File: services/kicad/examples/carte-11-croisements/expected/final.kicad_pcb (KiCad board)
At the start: 2 copper layers, 90 x 60 mm, 6 parts, among them J1 BUS_A, J2 BUS_B

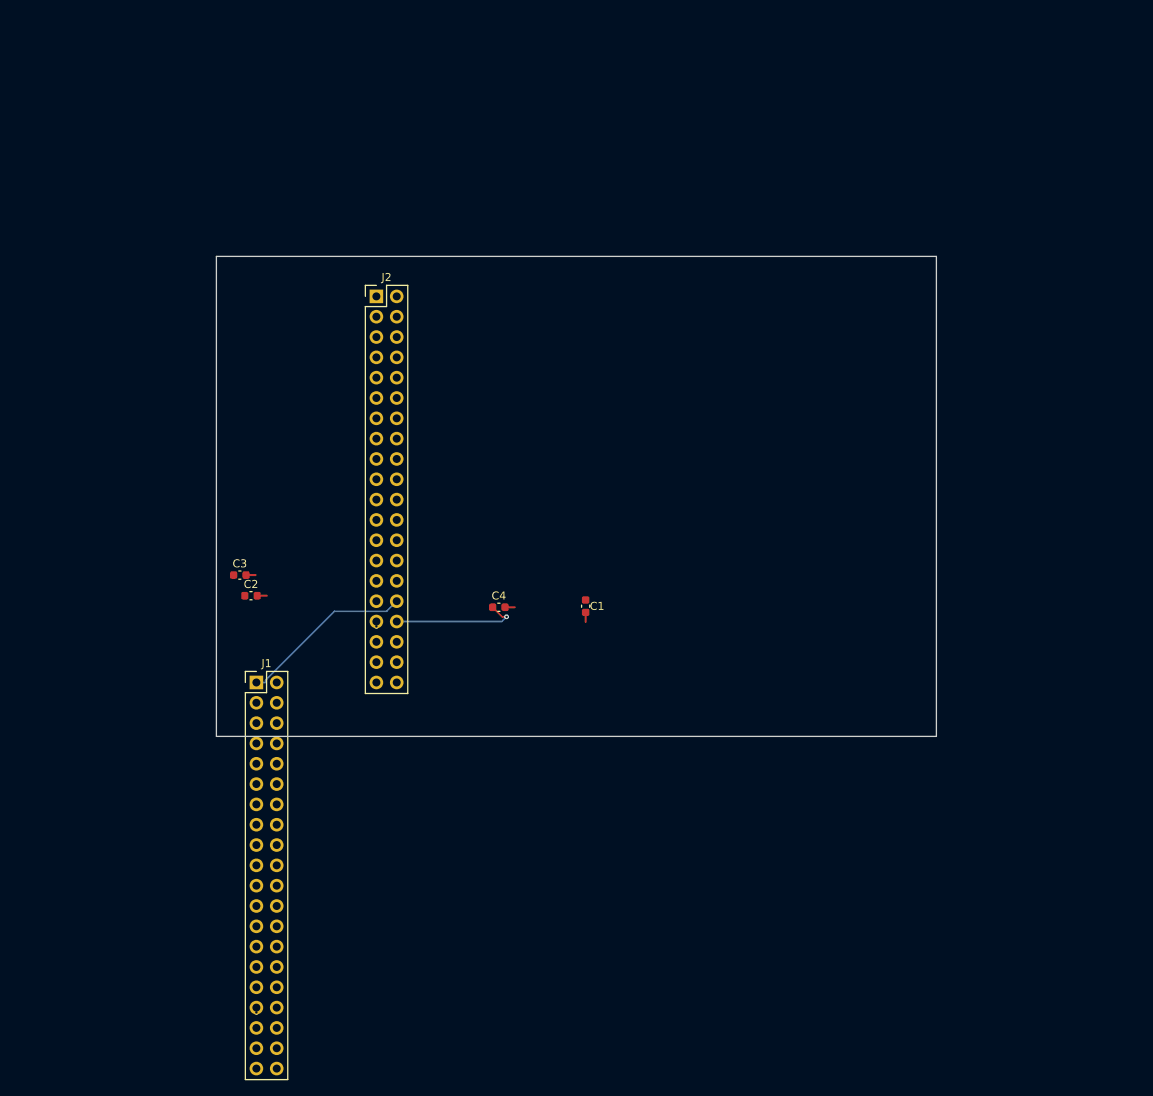
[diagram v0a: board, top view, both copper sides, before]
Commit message: feat(kicad): placement pro et routage 100 % fabricable sur les 16 cartes -- integration sur main (#164)
Branche d'integration coupee depuis origin/main (fab2a82, PR #162) : les
fichiers cles de main etaient des instantanes de feat/placement-seed-snap-
bypass (routing.py = 7981019, placement.py = 437a8b4...). On reprend donc
l'arbre entier de cette branche (345 commits, dernier 9f48667) et on y
conserve ce que main seul apportait :
- tools/verrou_routage.py + son test : « 6,2 Go par routage » rectifie
  (0,2 Go mesure ; c'est la concurrence qui emballe la memoire) ;
- tests/test_driver_llm_resync.py ;
- CLAUDE.md, PLAN.md, DECISIONS.md : fusion a trois voies, les sections
  des deux lignes conservees (2026-09-05 conteneur/verrou, 2026-09-07
  parcours asynchrone et chaine du driver, 2026-09-09/10 lecons).
Les skills *-delegate restent supprimes (remplaces le 2026-08-30).

Contenu : banc en deux phases (placement valide puis routage gele), snap
sur les regles natives, repli GND cible, journal Freerouting incremental,
horloge sans progres, via d'echappement vers le plan principal,
serigraphie degagee ; 16 cartes livrees a 100 %, 0 erreur DRC.

Verification : pytest services/kicad 1805 passed, 16 skipped ;
pnpm type-check 8/8.


Claude-Session: https://claude.ai/code/session_01TnMqm4La2CxQHHB5K8aSSV

Co-authored-by: Claude Fable 5.1 <noreply@anthropic.com>
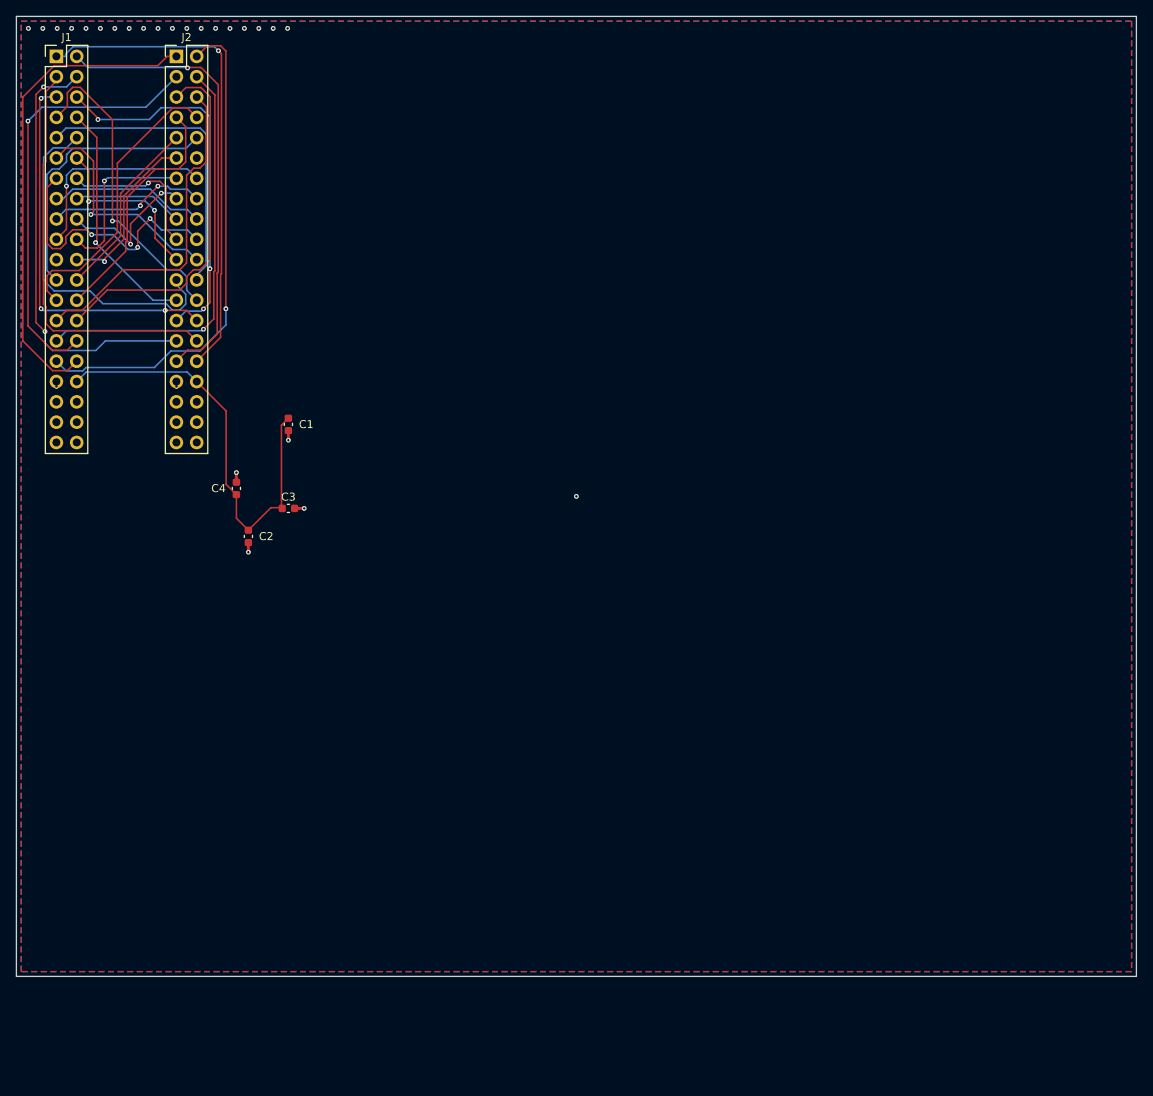
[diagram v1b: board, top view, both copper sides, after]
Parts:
- moved J1 82.2 mm to (83.5, 50.0)
- moved C1 43.6 mm to (112.5, 96.0)
- moved J2 39.1 mm to (98.5, 50.0)
- moved C4 36.0 mm to (106.0, 104.0), turned to 90 degrees
- moved C3 10.3 mm to (112.5, 106.5)
- moved C2 7.42 mm to (107.5, 110.0), turned to -90 degrees
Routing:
- net X31: track 0.00 -> 62.8 mm, vias 0 -> 1
- net X32: track 0.00 -> 60.5 mm
- net X02: track 0.00 -> 56.9 mm, vias 0 -> 1
- net X04: track 0.00 -> 54.9 mm, vias 0 -> 2
- net X30: track 0.00 -> 54.3 mm, vias 0 -> 1
- net X29: track 0.00 -> 52.1 mm, vias 0 -> 1
- net X03: track 0.00 -> 51.4 mm
- net X05: track 0.00 -> 48.5 mm, vias 0 -> 3
- net X06: track 0.00 -> 47.3 mm, vias 0 -> 3
- net X28: track 0.00 -> 45.9 mm
- net X10: track 0.00 -> 43.6 mm
- net X27: track 0.00 -> 42.0 mm
- net X07: track 0.00 -> 39.5 mm, vias 0 -> 1
- net X01: track 21.9 -> 61.4 mm, vias 0 -> 1
- net X09: track 0.00 -> 38.3 mm
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- added copper zone on B.Cu, net GND
- added copper zone on F.Cu, net GND
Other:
- board size 90 x 60 mm -> 140 x 120 mm
- copper layers 2 -> 4

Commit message: banc(rejeu): douze cartes hors le banc des dix, et le trou qu elles ont revele
Demande : refaire placement et routage de toutes les cartes d `examples/`
SAUF les dix du banc, sans toucher `stm32-validation` ni `STM32-Test`.

DOUZE CARTES REJOUEES, DEUX FAMILLES.

  groupe A (input/schema.json)        regenerer_le_banc.py — garde le meilleur
      carte-11-croisements            100 % · 0 err · 0 perdu   GARDE
      driver-clignotant-ne555         100 % · 0 err · 0 perdu   GARDE
      driver-stm32-minimal            100 % · 0 err · 0 perdu   GARDE
      driver-thermometre-i2c          100 % · 0 err · 0 perdu   GARDE

  groupe B (input/circuit.json)       banc_exemples.py — ecrit dans output/
      arduino-uno       2 couches  100 %  0 manq  0 err    925 s
      esp32-baseline    2 couches  100 %  0 manq  0 err    387 s
      led-blinker       2 couches  100 %  0 manq  0 err    124 s
      nucleo-f401       4 couches   98 %  1 manq  0 err   1814 s
      stm32-baseline    2 couches  100 %  0 manq  0 err    193 s
      stm32-30          2 couches  100 %  0 manq  0 err    404 s
      stm32-60          2 couches  100 %  0 manq  0 err    414 s
      stm32-100         2 couches  100 %  0 manq  0 err    308 s

LE REJEU CONFIRME LES BOARDS LIVRES — ON NE REMPLACE RIEN.

DRC des boards VERSIONNES face aux boards du rejeu, meme instrument
(`kicad-cli pcb drc --severity-all`) des deux cotes :

      sept cartes            0 err · 0 manq des DEUX cotes   egalite
      nucleo-f401            0 manq versionne, 1 au rejeu    on garde l ancien

Livrer des boards de qualite identique ferait du bruit sans rien apporter, et
le tirage de `nucleo-f401` est moins bon : la protection a joue exactement
comme prevu.

LE TROU : CES HUIT CARTES N AVAIENT AUCUN `mesures.json`.

Leur board etait livre depuis le 2026-09-07 et RIEN ne disait ce qu il valait.
Un lecteur ne pouvait ni le verifier ni s en apercevoir — c est la faute que ce
depot poursuit partout, appliquee non pas a un compteur mais a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
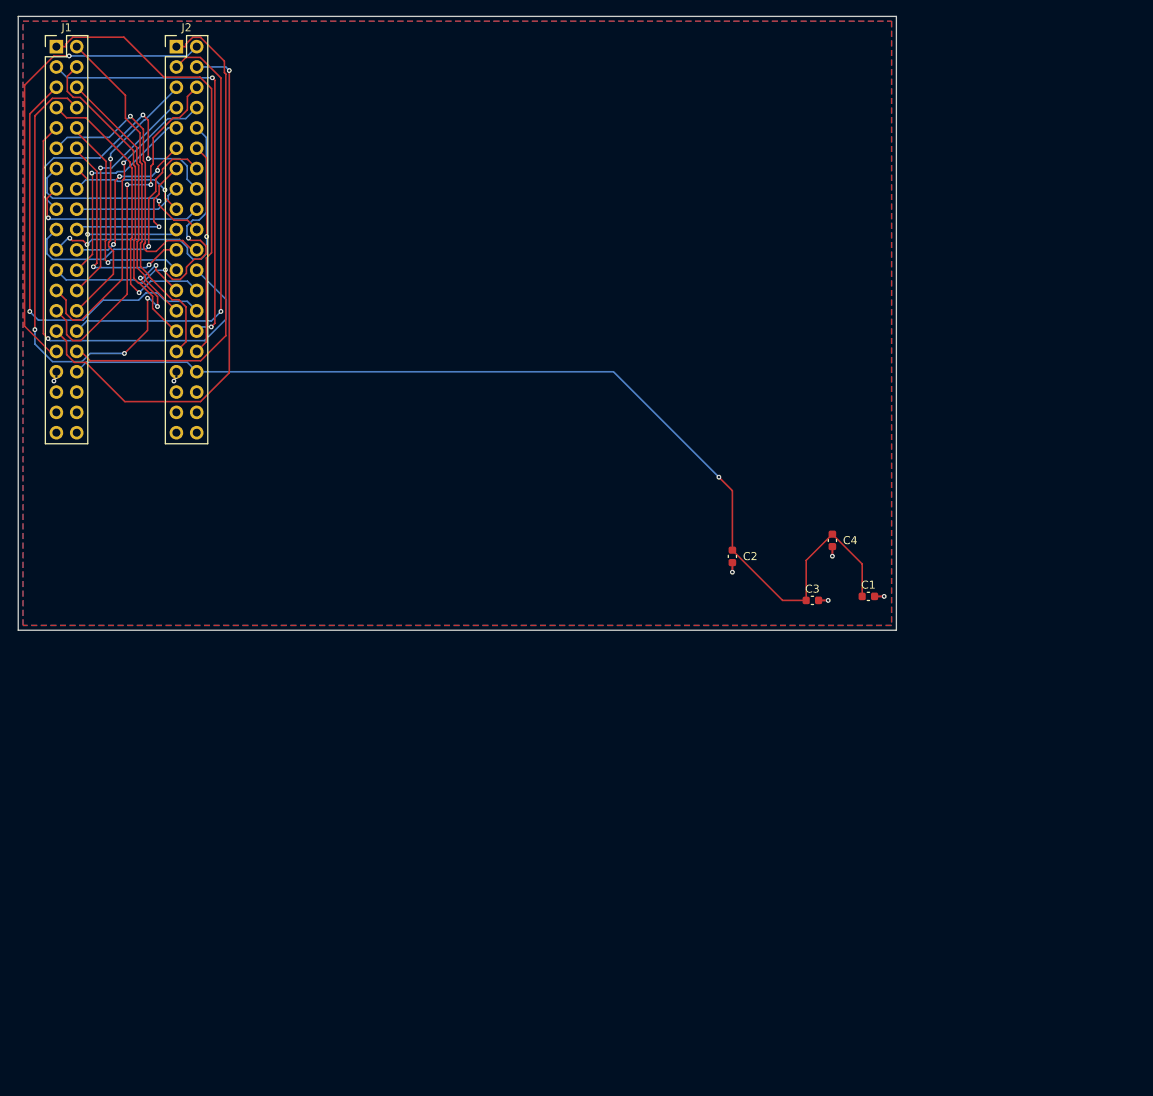
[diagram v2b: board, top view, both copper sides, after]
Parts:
- moved C1 75.6 mm to (185.0, 117.5), turned to 0 degrees
- moved C4 74.8 mm to (180.5, 110.5), turned to -90 degrees
- moved C3 66.5 mm to (178.0, 118.0)
- moved C2 60.6 mm to (168.0, 112.5)
- moved J1 1.22 mm to (83.5, 48.8)
- moved J2 1.22 mm to (98.5, 48.8)
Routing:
- net +3V3: track 54.2 -> 127.3 mm, vias 0 -> 1
- net X08: track 29.9 -> 68.7 mm, vias 1 -> 6
- net X09: track 38.3 -> 58.4 mm, vias 0 -> 1
- net X29: track 52.1 -> 69.8 mm
- net X10: track 43.6 -> 27.8 mm, vias 0 -> 1
- net X17: track 20.0 -> 35.3 mm
- net X04: track 54.9 -> 40.0 mm, vias 2 -> 0
- net X06: track 47.3 -> 33.2 mm, vias 3 -> 0
- net X28: track 45.9 -> 33.6 mm, vias 0 -> 1
- net X02: track 56.9 -> 44.9 mm, vias 1 -> 0
- net X21: track 23.8 -> 35.4 mm, vias 0 -> 3
- net X13: track 33.9 -> 24.4 mm, vias 3 -> 1
- net X11: track 28.2 -> 36.1 mm
- net X19: track 25.6 -> 32.8 mm
- net X23: track 34.8 -> 41.9 mm, vias 0 -> 2
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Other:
- board size 140 x 120 mm -> 109.8 x 76.7 mm
- copper layers 4 -> 2

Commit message: banc(preuve): 22 cartes sur 22 a 100 % routees et fabricables, placement gele
Objectif utilisateur, 2026-09-24 : « une solution generale — 100 % route,
100 % fabricable ; si on n atteint pas 100 %, on escalade le nombre de couches,
et on doit l atteindre ».

METHODE. Chaque carte part de son placement VERSIONNE, gele : seuls le code de
routage et le juge changent — un resultat ne peut pas venir du hasard du
placement. Voie HTTP de production, service redemarre pour charger le nouveau
code, `/tmp/cirqix-reglages.json` supprime et verifie absent. Juge :
`tools.drc.est_bloquante`.

RESULTAT : 22 / 22 — 100 % routees, 0 violation bloquante, 0 connexion
manquante, 0 percage fautif. 4481 s au total. stm32-validation et STM32-Test
exclus a la demande de l utilisateur.

L ESCALADE ATTEINT 100 %, ET LE JOURNAL DIT POURQUOI.

    nucleo-f401   palier 4 : tirage PROTEGE ->   0 %   tirage LIBRE -> 100 %
    carte-10      palier 4 : tirage PROTEGE ->  95 %   tirage LIBRE -> 100 %

Deux cartes, deux escalades reelles, le meme mecanisme qui decide. La veille,
nucleo-f401 avait donne a 4 couches 98, 98, fige, fige, 96 — jamais 100 —
parce que les trois tirages du palier etaient proteges.

UN SEUL BOARD VERSIONNE REMPLACE : carte-11-croisements.

Rejuge avec le juge corrige, le board du 2026-09-23 portait 4 violations
hole_to_hole BLOQUANTES — deux vias dans le percage de J1.33 et J2.33 a
-0,050 mm — et son mesures.json disait `"fabricable": true`. Le nouveau board
est propre, sur 4 couches au lieu de 2 ; mesures et rendu RECALCULES depuis le
board, jamais recopies. Les 21 autres boards versionnes passent le juge corrige
et restent tels quels.

⚠️ CE QUE CE BANC NE PROUVE PAS : un placement « pro ». Le rendu de carte-11
le montre — six composants sur 110 x 77 mm, les connecteurs serres dans un
coin, les condensateurs isoles a l autre bout, une carte presque vide. Le
routage y est propre, le placement non. Ce banc isole le routage a placement
gele ; il ne dit rien du placement.

⚠️ U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
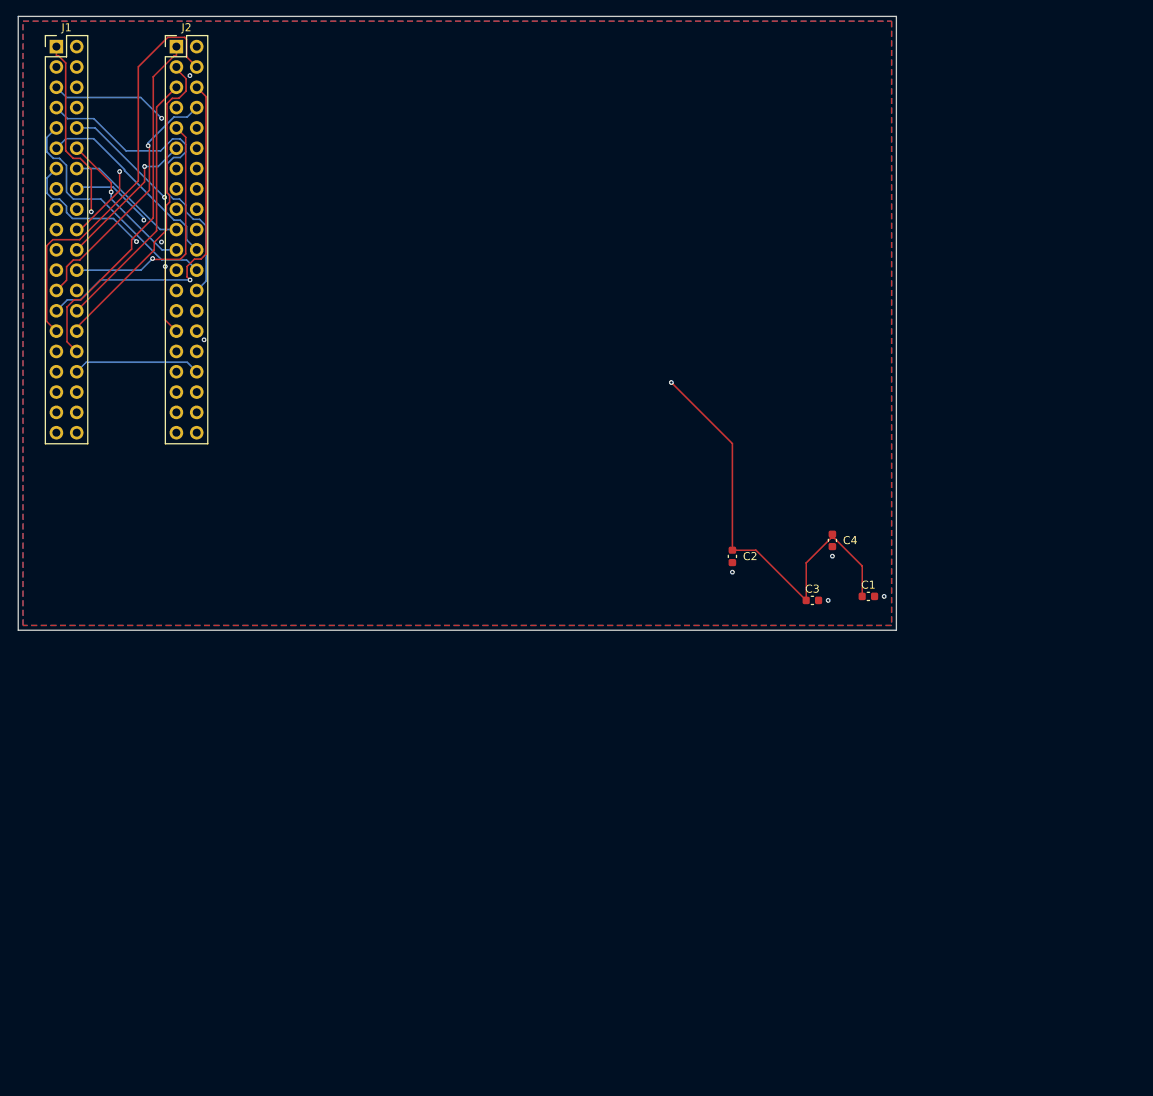
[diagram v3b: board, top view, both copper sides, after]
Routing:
- net X08: track 68.7 -> 28.0 mm, vias 6 -> 0
- net X09: track 58.4 -> 30.3 mm, vias 1 -> 0
- net X29: track 69.8 -> 51.9 mm, vias 1 -> 0
- net X32: track 62.7 -> 44.9 mm
- net X17: track 35.3 -> 19.6 mm, vias 2 -> 0
- net X30: track 55.3 -> 39.9 mm, vias 1 -> 0
- net X11: track 36.1 -> 24.8 mm, vias 1 -> 0
- net X01: track 56.3 -> 47.0 mm, vias 0 -> 1
- net X12: track 27.4 -> 18.9 mm, vias 2 -> 1
- net GND: track 8.40 -> 0.00 mm, vias 8 -> 4
- net X25: track 39.6 -> 31.7 mm
- net X21: track 35.4 -> 29.6 mm, vias 3 -> 0
- net X23: track 41.9 -> 36.2 mm, vias 2 -> 0
- net X07: track 37.2 -> 42.5 mm, vias 1 -> 0
- net X24: track 25.9 -> 30.8 mm
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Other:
- copper layers 2 -> 4
